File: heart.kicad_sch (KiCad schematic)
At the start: 37 parts, among them SW1 SW_MEC_5E, SW2 SW_SPST, U1 ATtiny13A-P

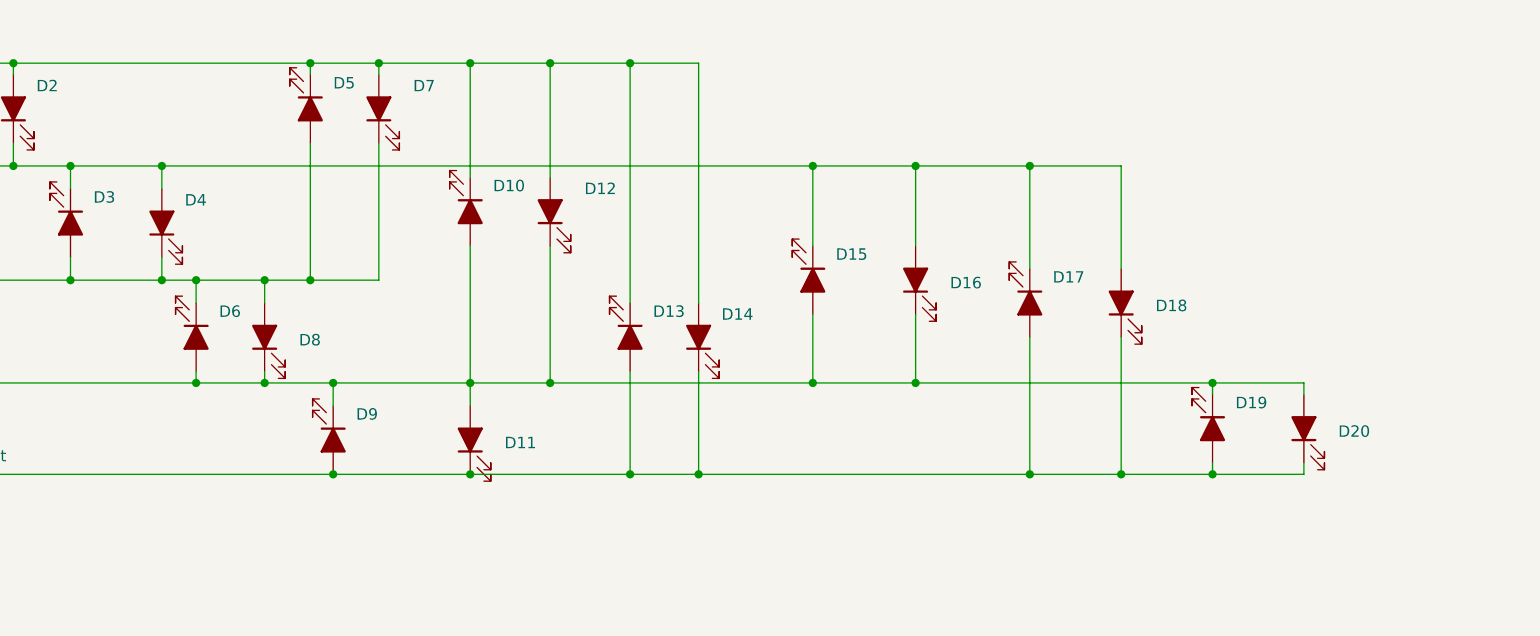
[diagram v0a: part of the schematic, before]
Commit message: Changed two bad connections on LED.
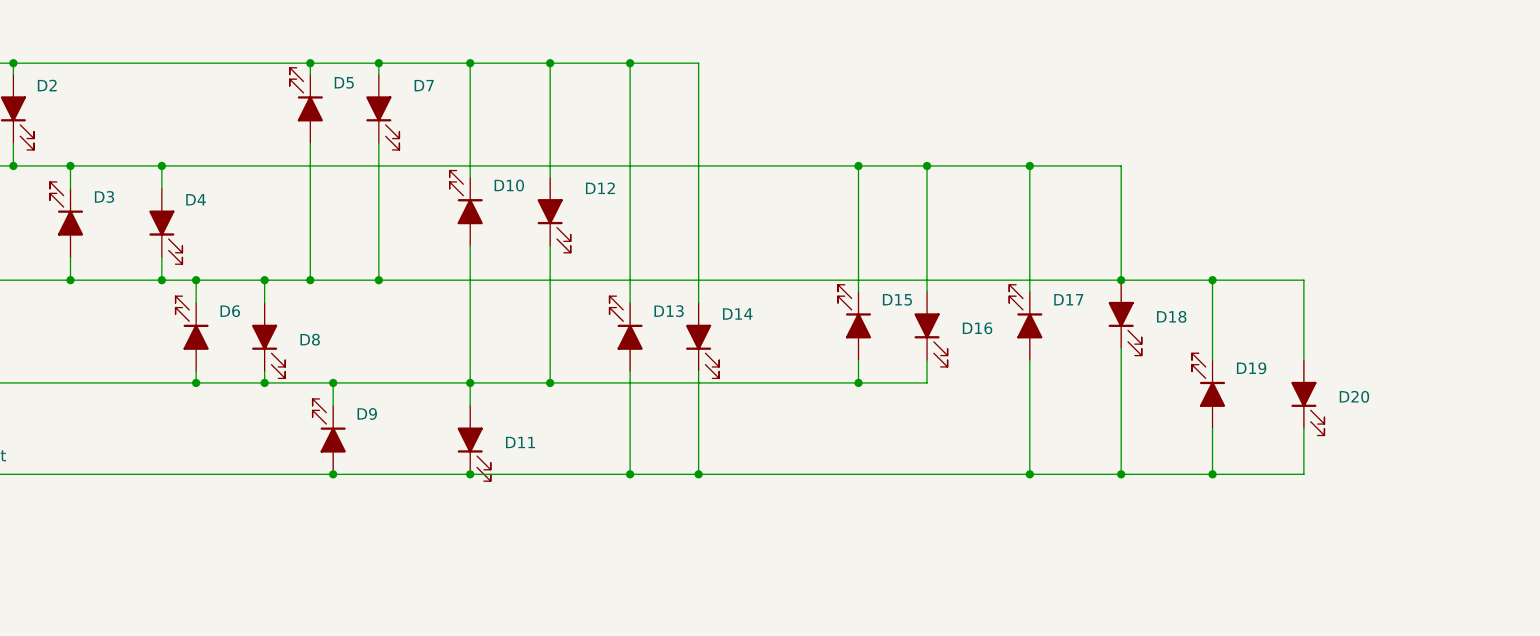
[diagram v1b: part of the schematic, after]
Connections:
- net at D10.2 (A), D11.2 (A), D12.1 (K)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: no longer D19.1 (K), D20.2 (A)
- net at D1.2 (A), D15.1 (K), D16.2 (A)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: now also D19.1 (K), D20.2 (A), D3.2 (A), D4.1 (K), D5.2 (A), D6.1 (K), D7.1 (K), D8.2 (A), R3.2, TP3.1
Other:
- moved on the sheet: D15, D16, D17, D18, D19, D20
